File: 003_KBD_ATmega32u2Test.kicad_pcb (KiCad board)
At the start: 2 copper layers, 95 x 26 mm, 10 parts

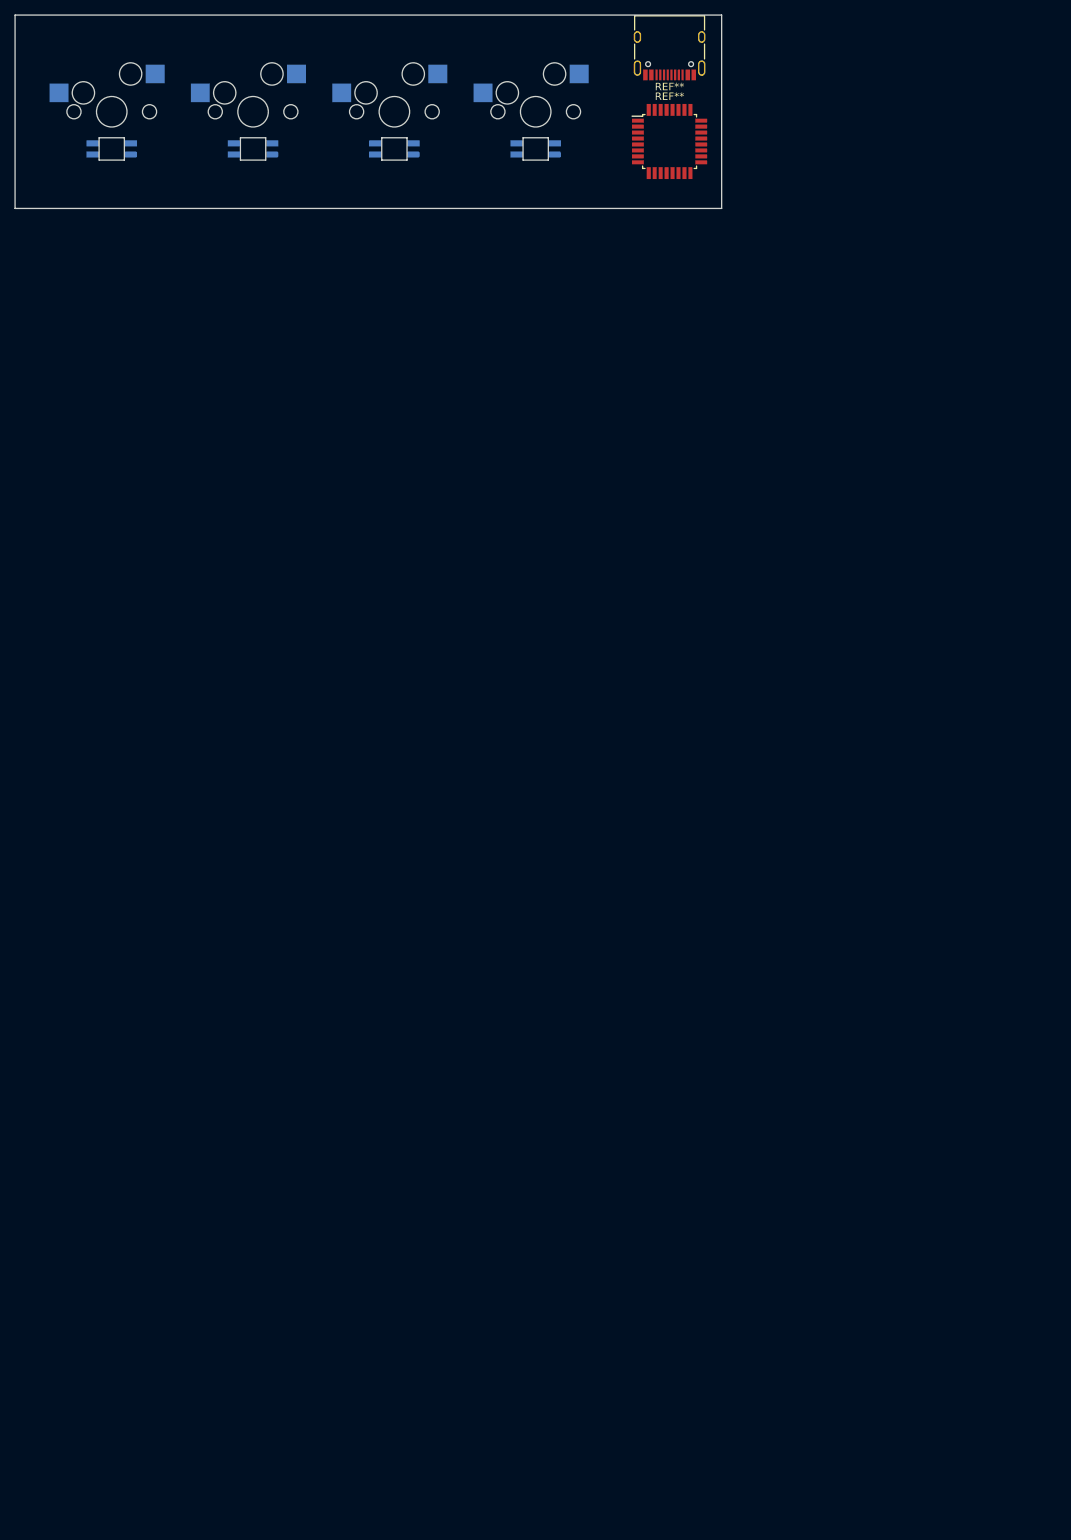
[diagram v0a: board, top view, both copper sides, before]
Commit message: 回路図の更新(ATMEGA32U4へ変更、OLED追加)
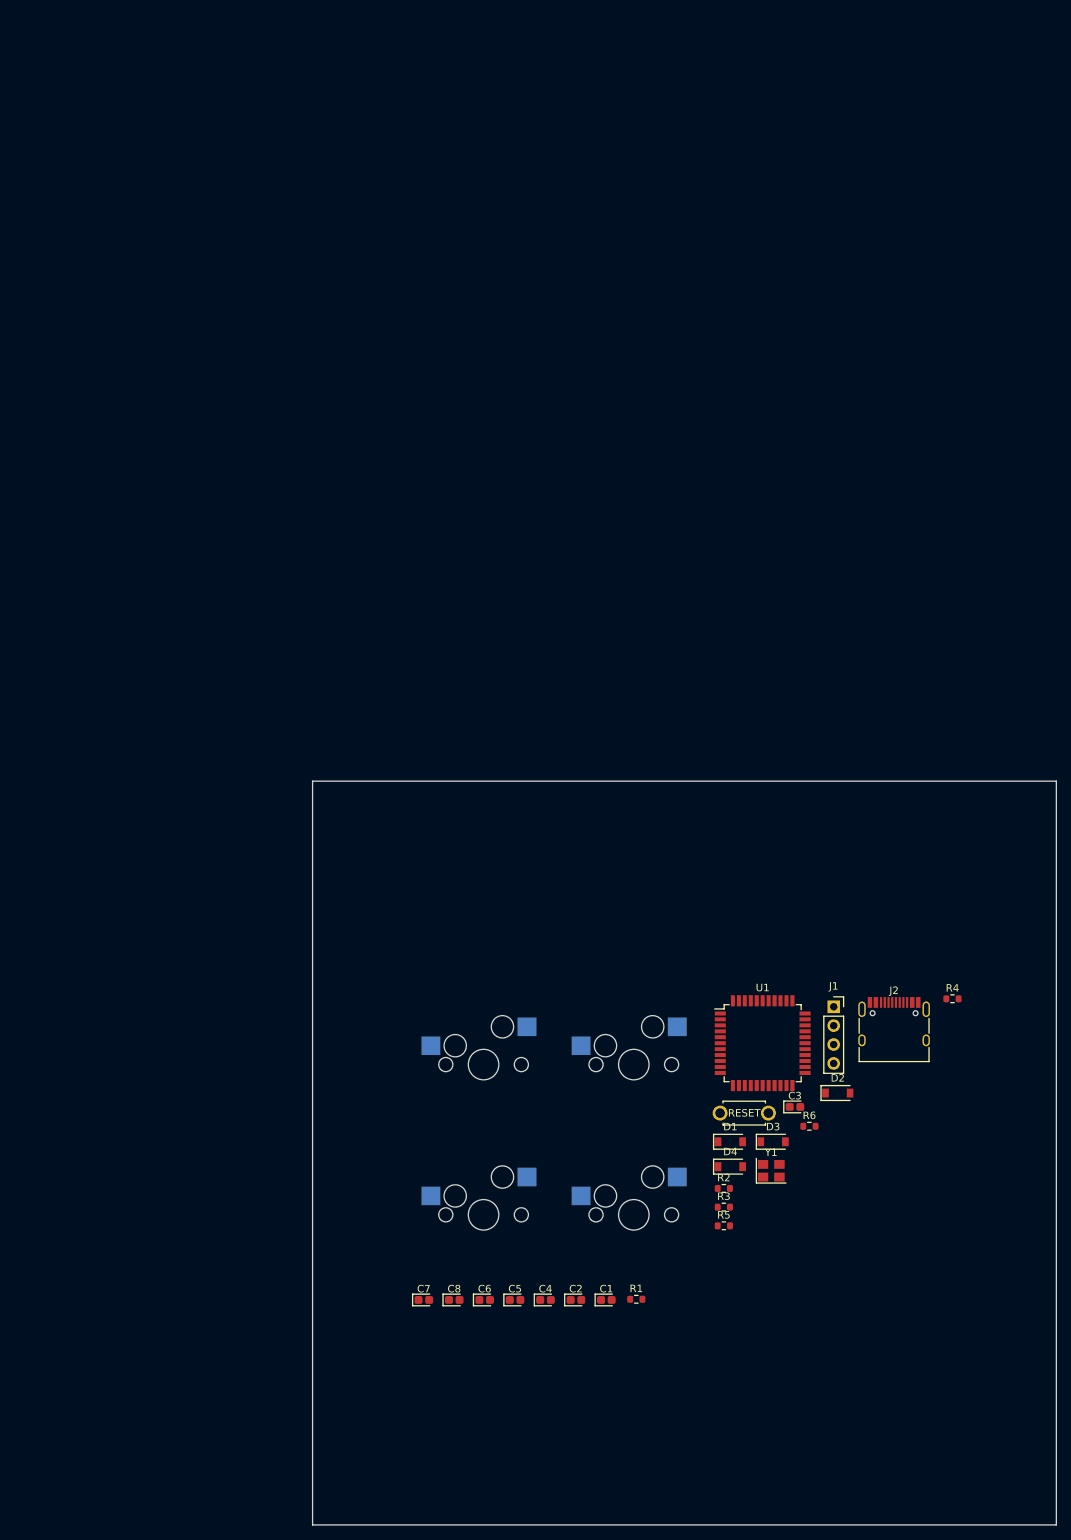
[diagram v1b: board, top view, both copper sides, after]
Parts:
- removed REF**: USB_C_5077CR, KBD_MyFavorite:USB_C_5077CR
- removed REF** (x4): KEY_SWITCH, KBD_foostan:CherryMX_Hotswap
- removed REF**: ATMega32U2, KBD_MyFavorite:ATMega32U2
- removed REF** (x4): SK6812-MINI-E, KBD_MyFavorite:SK6812-MINI-E
- added C1: 1u, Capacitor_Tantalum_SMD:CP_EIA-1608-08_AVX-J, F.Cu at (94.5, 109.8)
- added C2: 0.1u, Capacitor_Tantalum_SMD:CP_EIA-1608-08_AVX-J, F.Cu at (90.4, 109.8)
- added C3: 0.1u, Capacitor_Tantalum_SMD:CP_EIA-1608-08_AVX-J, F.Cu at (119.9, 83.8)
- added C4: 0.1u, Capacitor_Tantalum_SMD:CP_EIA-1608-08_AVX-J, F.Cu at (86.3, 109.8)
- added C5: 0.1u, Capacitor_Tantalum_SMD:CP_EIA-1608-08_AVX-J, F.Cu at (82.2, 109.8)
- added C6: 4.7u, Capacitor_Tantalum_SMD:CP_EIA-1608-08_AVX-J, F.Cu at (78.1, 109.8)
- added C7: 9p, Capacitor_Tantalum_SMD:CP_EIA-1608-08_AVX-J, F.Cu at (70.0, 109.8)
- added C8: 9p, Capacitor_Tantalum_SMD:CP_EIA-1608-08_AVX-J, F.Cu at (74.0, 109.8)
- added D1: D, Diode_SMD:D_SOD-123, F.Cu at (111.2, 88.5)
- added D2: D, Diode_SMD:D_SOD-123, F.Cu at (125.6, 81.9)
- added D3: D, Diode_SMD:D_SOD-123, F.Cu at (116.9, 88.5)
- added D4: D, Diode_SMD:D_SOD-123, F.Cu at (111.2, 91.8)
- added J1: Conn_01x04_Male, Connector_PinSocket_2.54mm:PinSocket_1x04_P2.54mm_Vertical, F.Cu at (125.1, 70.3)
- added J2: USB_C_Receptacle_USB2.0, Connector_USB:USB_C_Receptacle_HRO_TYPE-C-31-M-12, F.Cu at (133.2, 73.8)
- added R1: 10k, Resistor_SMD:R_0603_1608Metric, F.Cu at (98.5, 109.7)
- added R2: 10k, Resistor_SMD:R_0603_1608Metric, F.Cu at (110.3, 94.8)
- added R3: 5.1k, Resistor_SMD:R_0603_1608Metric, F.Cu at (110.3, 97.3)
- added R4: 5.1k, Resistor_SMD:R_0603_1608Metric, F.Cu at (141.0, 69.3)
- added R5: 22, Resistor_SMD:R_0603_1608Metric, F.Cu at (110.3, 99.8)
- added R6: 22, Resistor_SMD:R_0603_1608Metric, F.Cu at (121.8, 86.4)
- added RST1: SW_PUSH, KBD_foostan:ResetSW_1side, F.Cu at (113.0, 84.6)
- added SW1: SW_PUSH, KBD_foostan:CherryMX_Hotswap, F.Cu at (98.2, 98.3)
- added SW2: SW_PUSH, KBD_foostan:CherryMX_Hotswap, F.Cu at (98.2, 78.1)
- added SW3: SW_PUSH, KBD_foostan:CherryMX_Hotswap, F.Cu at (78.0, 98.3)
- added SW4: SW_PUSH, KBD_foostan:CherryMX_Hotswap, F.Cu at (78.0, 78.1)
- added U1: ATmega32U4-AU, Package_QFP:TQFP-44_10x10mm_P0.8mm, F.Cu at (115.5, 75.2)
- added Y1: Crystal_GND24, Crystal:Crystal_SMD_3225-4Pin_3.2x2.5mm, F.Cu at (116.7, 92.4)
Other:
- board size 95 x 26 mm -> 100 x 100 mm
